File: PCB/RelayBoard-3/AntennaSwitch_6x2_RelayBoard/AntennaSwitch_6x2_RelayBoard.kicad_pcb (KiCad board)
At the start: 2 copper layers, 200 x 90 mm, 41 parts, among them J1 Conn_Coaxial, J10 Conn_01x08, J2 Conn_Coaxial, J3 Conn_Coaxial, J4 Conn_Coaxial, J5 Conn_Coaxial, J6 Conn_Coaxial, J7 Conn_Coaxial, J8 Conn_Coaxial, J9 Conn_01x08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

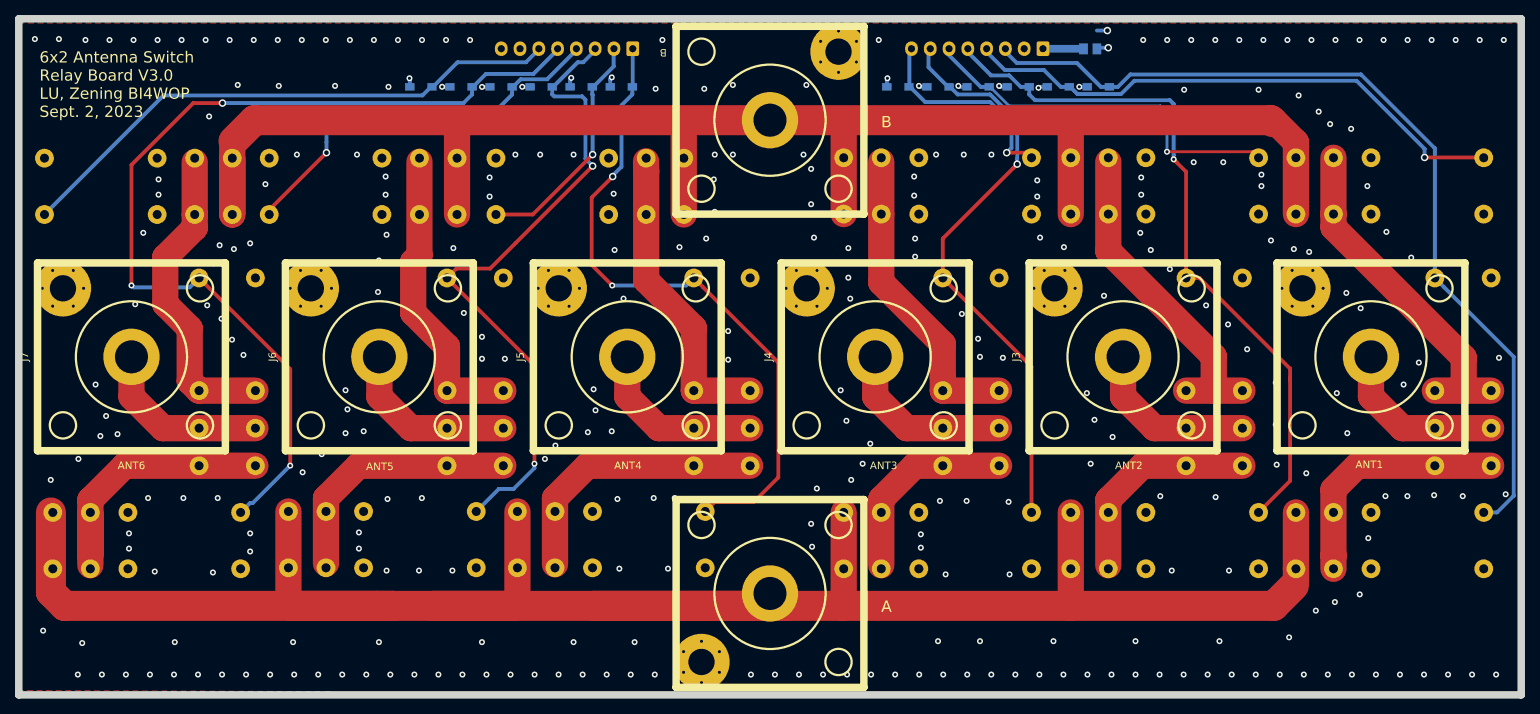
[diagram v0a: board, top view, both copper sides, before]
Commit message: Start to add support for WebSocket
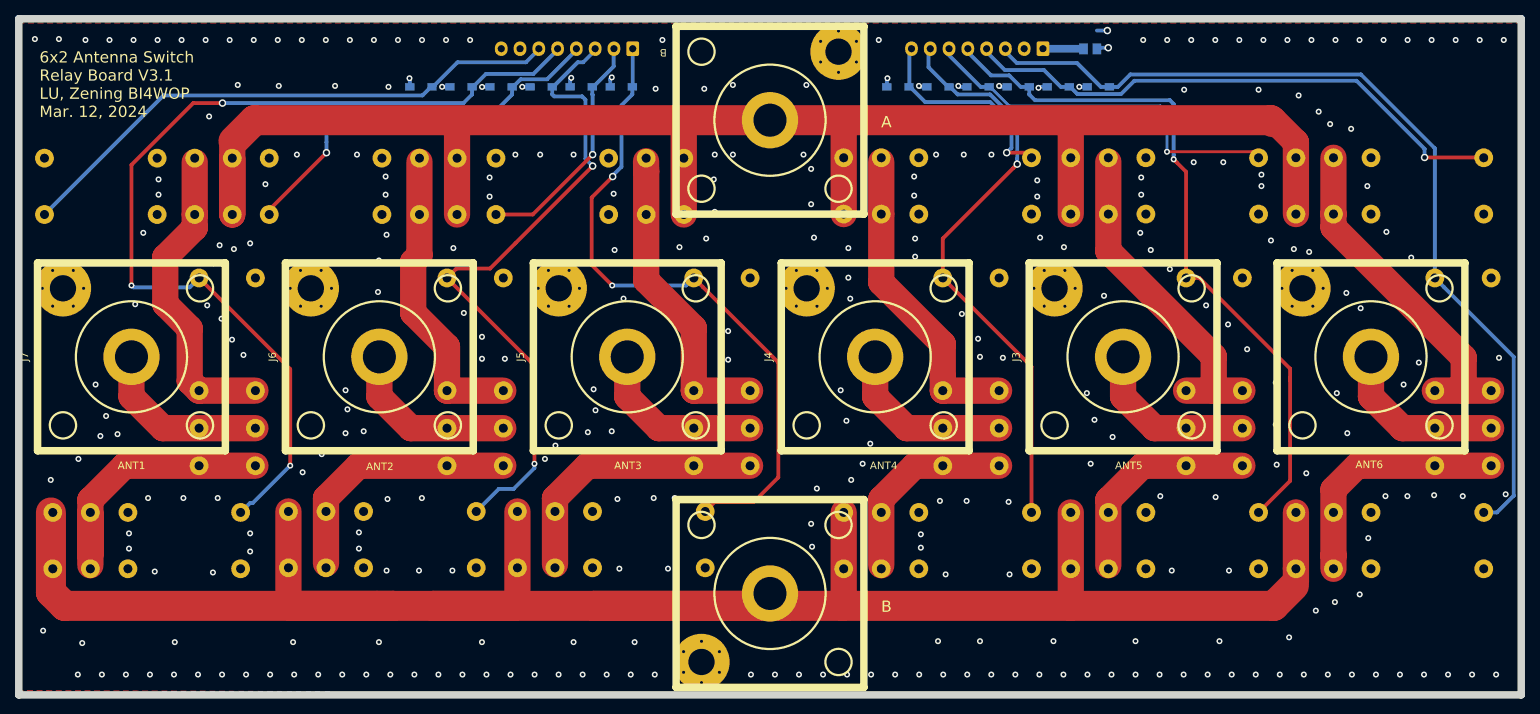
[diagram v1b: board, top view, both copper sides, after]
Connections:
- net /SEL1_4 renamed /SEL2_3
- net /SEL1_5 renamed /SEL2_2
- net /SEL1_6 renamed /SEL2_1
- J1 pad 1: A -> B
- J2 pad 1: /ANT1 -> /ANT6
- J3 pad 1: /ANT2 -> /ANT5
- J4 pad 1: /ANT3 -> /ANT4
- J5 pad 1: /ANT4 -> /ANT3
- J6 pad 1: /ANT5 -> /ANT2
- J7 pad 1: /ANT6 -> /ANT1
- J8 pad 1: B -> A
- K1 pad 3: /ANT1_A -> /ANT6_A
- K1 pad 4: A -> B
- K1 pad 5: A -> B
- K1 pad 6: /ANT1_A -> /ANT6_A
- K10 pad 2: /ANT4_B -> /ANT3_B
- K10 pad 3: /ANT4 -> /ANT3
- K10 pad 4: /ANT4_A -> /ANT3_A
- K10 pad 5: /ANT4_A -> /ANT3_A
- K10 pad 6: /ANT4 -> /ANT3
- K10 pad 7: /ANT4_B -> /ANT3_B
- K11 pad 2: /ANT5_B -> /ANT2_B
- K11 pad 3: /ANT5 -> /ANT2
- K11 pad 4: /ANT5_A -> /ANT2_A
- K11 pad 5: /ANT5_A -> /ANT2_A
- K11 pad 6: /ANT5 -> /ANT2
- K11 pad 7: /ANT5_B -> /ANT2_B
- K12 pad 2: /ANT6_B -> /ANT1_B
- K12 pad 3: /ANT6 -> /ANT1
- K12 pad 4: /ANT6_A -> /ANT1_A
- K12 pad 5: /ANT6_A -> /ANT1_A
- K12 pad 6: /ANT6 -> /ANT1
- K12 pad 7: /ANT6_B -> /ANT1_B
- K13 pad 3: /ANT1_B -> /ANT6_B
- K13 pad 4: B -> A
- K13 pad 5: B -> A
- K13 pad 6: /ANT1_B -> /ANT6_B
- K14 pad 3: /ANT2_B -> /ANT5_B
- K14 pad 4: B -> A
- K14 pad 5: B -> A
- K14 pad 6: /ANT2_B -> /ANT5_B
- K15 pad 3: /ANT3_B -> /ANT4_B
- K15 pad 4: B -> A
- K15 pad 5: B -> A
- K15 pad 6: /ANT3_B -> /ANT4_B
- K16 pad 3: /ANT4_B -> /ANT3_B
- K16 pad 4: B -> A
- K16 pad 5: B -> A
- K16 pad 6: /ANT4_B -> /ANT3_B
- K17 pad 3: /ANT5_B -> /ANT2_B
- K17 pad 4: B -> A
- K17 pad 5: B -> A
- K17 pad 6: /ANT5_B -> /ANT2_B
- K18 pad 3: /ANT6_B -> /ANT1_B
- K18 pad 4: B -> A
- K18 pad 5: B -> A
- K18 pad 6: /ANT6_B -> /ANT1_B
- K2 pad 3: /ANT2_A -> /ANT5_A
- K2 pad 4: A -> B
- K2 pad 5: A -> B
- K2 pad 6: /ANT2_A -> /ANT5_A
- K3 pad 3: /ANT3_A -> /ANT4_A
- K3 pad 4: A -> B
- K3 pad 5: A -> B
- K3 pad 6: /ANT3_A -> /ANT4_A
- K4 pad 3: /ANT4_A -> /ANT3_A
- K4 pad 4: A -> B
- K4 pad 5: A -> B
- K4 pad 6: /ANT4_A -> /ANT3_A
- K5 pad 3: /ANT5_A -> /ANT2_A
- K5 pad 4: A -> B
- K5 pad 5: A -> B
- K5 pad 6: /ANT5_A -> /ANT2_A
- K6 pad 3: /ANT6_A -> /ANT1_A
- K6 pad 4: A -> B
- K6 pad 5: A -> B
- K6 pad 6: /ANT6_A -> /ANT1_A
- K7 pad 2: /ANT1_B -> /ANT6_B
- K7 pad 3: /ANT1 -> /ANT6
- K7 pad 4: /ANT1_A -> /ANT6_A
- K7 pad 5: /ANT1_A -> /ANT6_A
- K7 pad 6: /ANT1 -> /ANT6
- K7 pad 7: /ANT1_B -> /ANT6_B
- K8 pad 2: /ANT2_B -> /ANT5_B
- K8 pad 3: /ANT2 -> /ANT5
- K8 pad 4: /ANT2_A -> /ANT5_A
- K8 pad 5: /ANT2_A -> /ANT5_A
- K8 pad 6: /ANT2 -> /ANT5
- K8 pad 7: /ANT2_B -> /ANT5_B
- K9 pad 2: /ANT3_B -> /ANT4_B
- K9 pad 3: /ANT3 -> /ANT4
- K9 pad 4: /ANT3_A -> /ANT4_A
- K9 pad 5: /ANT3_A -> /ANT4_A
- K9 pad 6: /ANT3 -> /ANT4
- K9 pad 7: /ANT3_B -> /ANT4_B
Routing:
- net B: track 219.7 -> 287.0 mm
- net A: track 287.0 -> 219.7 mm
- net /ANT4_A: track 36.6 -> 26.3 mm
- net /ANT3_A: track 26.3 -> 36.6 mm
- net /ANT5_A: track 34.1 -> 28.4 mm
- net /ANT2_A: track 28.4 -> 34.1 mm
- net /ANT6_A: track 38.3 -> 32.9 mm
- net /ANT1_A: track 32.9 -> 38.3 mm
- net /ANT6_B: track 41.4 -> 45.7 mm
- net /ANT1_B: track 45.7 -> 41.4 mm
- net /ANT5_B: track 40.2 -> 43.8 mm
- net /ANT2_B: track 43.8 -> 40.2 mm
- net /ANT4_B: track 40.7 -> 41.4 mm
- net /ANT3_B: track 41.4 -> 40.7 mm
- net /ANT5: track 23.5 -> 22.9 mm
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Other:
- board text added: "6x2 Antenna Switch Relay Board V3.1 LU, Zening BI4WOP Mar. 12, 2024"
- board text added: "Errata: V3.0 ANT6-ANT1 annotations are reversed, A and B are reversed"
- board text removed: "6x2 Antenna Switch Relay Board V3.0 LU, Zening BI4WOP Sept. 2, 2023"
